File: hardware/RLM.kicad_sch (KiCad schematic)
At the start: 24 parts, among them J1 Conn_01x03, J2 Conn_01x03, SW1 SW_Push, SW2 SW_Push, U3 AP1117-33, U7 MCP2562-E-SN

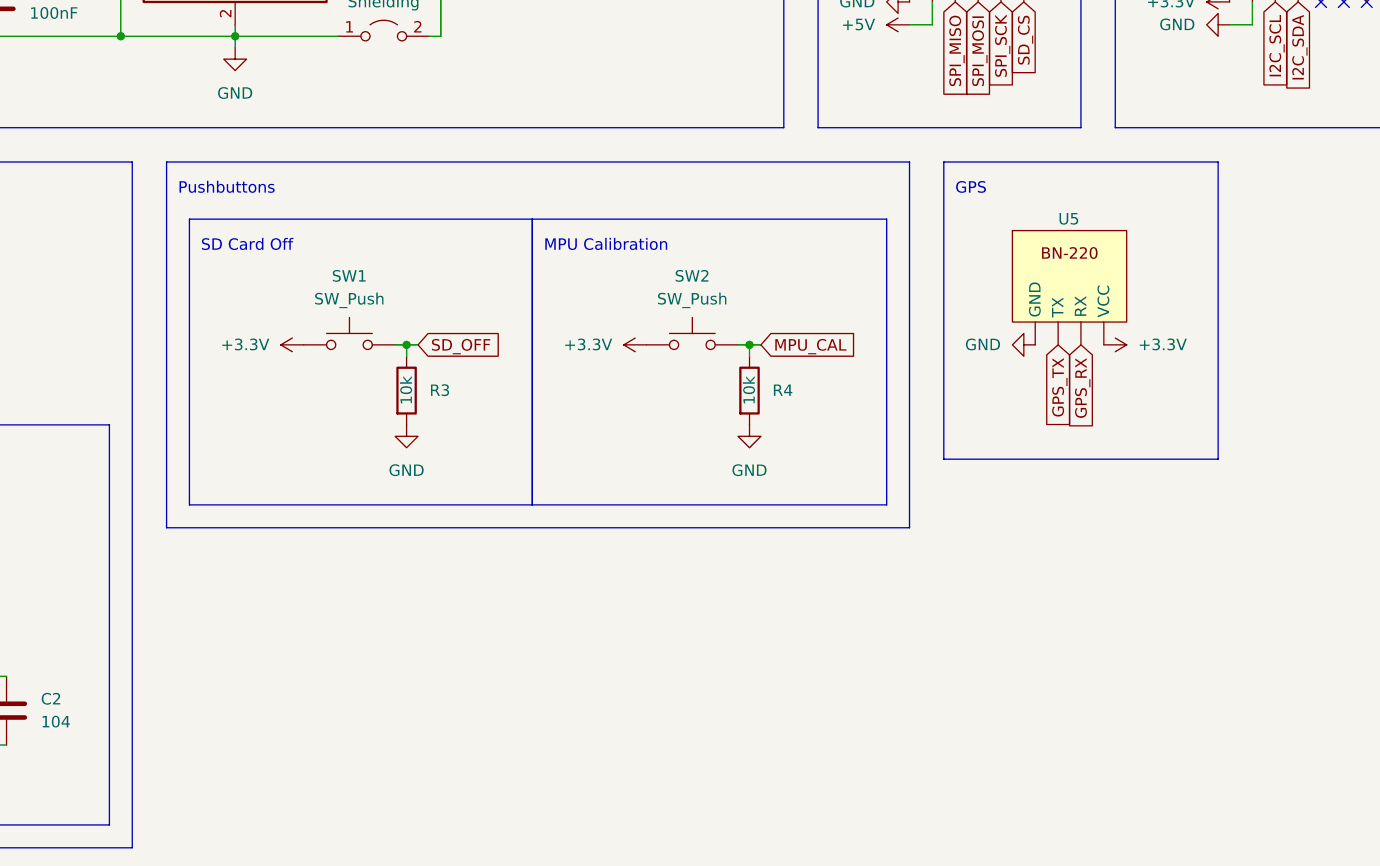
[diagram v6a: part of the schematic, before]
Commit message: feat: add mounting holes
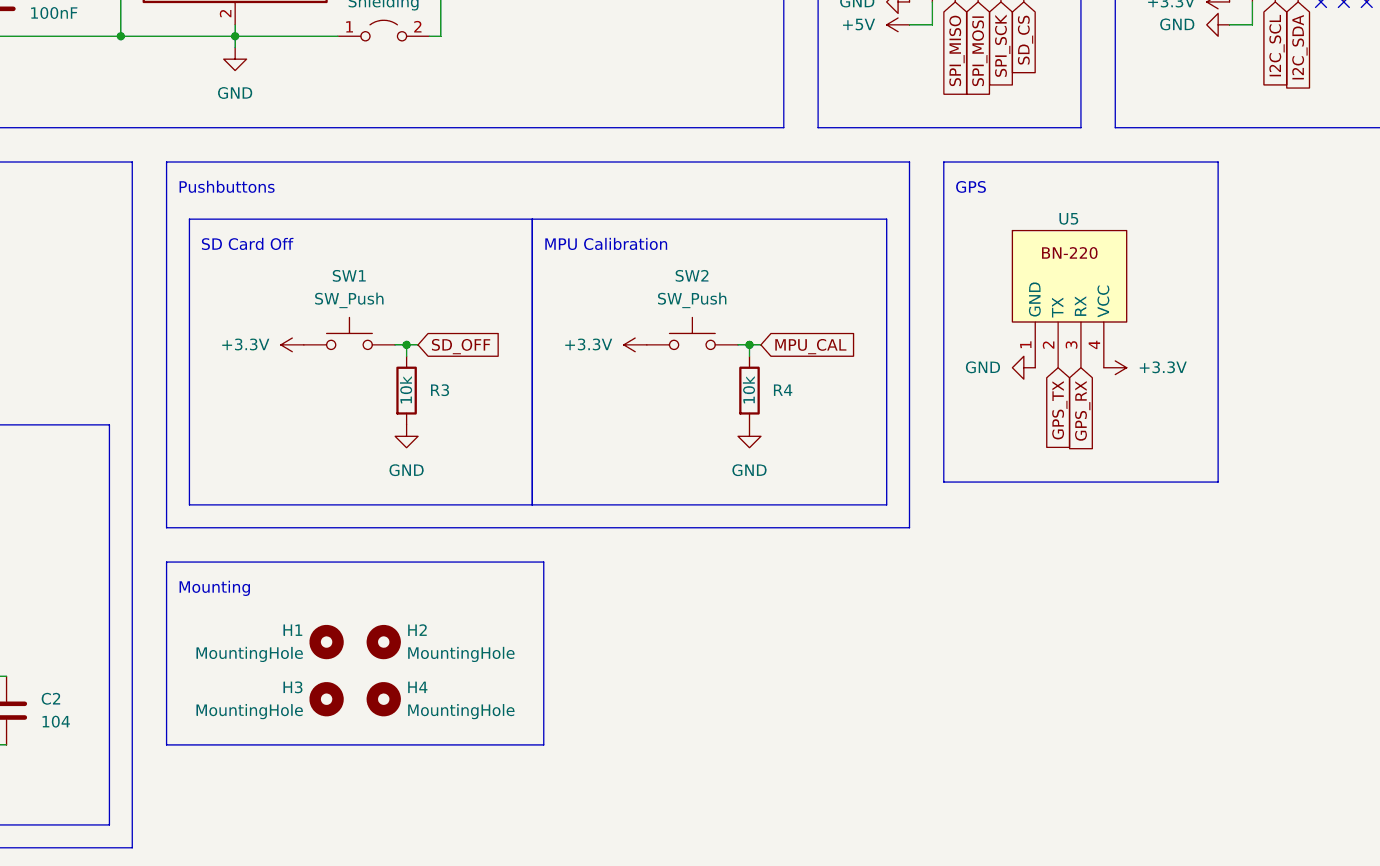
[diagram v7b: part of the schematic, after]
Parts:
- added H1, H2, H3, H4: MountingHole, MountingHole:MountingHole_4.3mm_M4, symbol Mechanical:MountingHole
- R3, R4: footprint (none) -> Resistor_SMD:R_0603_1608Metric
- U5: footprint (none) -> Connector_PinHeader_2.54mm:PinHeader_1x04_P2.54mm_Vertical
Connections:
- net +3.3V: now also U5.4 (VCC); no longer U5. (VCC)
- net GND: now also U5.1 (GND); no longer U5. (VCC)
- net GPS_RX: now also U5.3 (RX); no longer U5. (VCC)
- net GPS_TX: now also U5.2 (TX); no longer U5. (VCC)
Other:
- note added: "Mounting"
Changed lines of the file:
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@@
     (fill (type none))
   )
-  (rectangle (start 204.47 95.25) (end 234.95 128.27)
+  (rectangle (start 204.47 95.25) (end 234.95 130.81)
     (stroke (width 0) (type default))
     (fill (type none))
@@
     (fill (type none))
   )
+  (rectangle (start 118.11 139.7) (end 160.02 160.02)
+    (stroke (width 0) (type default))
+    (fill (type none))
+  )
   (rectangle (start 17.78 17.78) (end 76.2 91.44)
     (stroke (width 0) (type default))
@@
     (effects (font (size 1.27 1.27)) (justify left bottom))
   )
+  (text "Mounting" (at 119.38 143.51 0)
+    (effects (font (size 1.27 1.27)) (justify left bottom))
+  )
   (text "Accelerometer/Gyroscope" (at 224.79 55.88 0)
     (effects (font (size 1.27 1.27)) (justify left bottom))
@@
     )
   )
-  (global_label "GPS_RX" (shape input) (at 219.71 115.57 270) (fields_autoplaced)
-    (effects (font (size 1.27 1.27)) (justify right))
-    (property "Intersheetrefs" "${INTERSHEET_REFS}" (at 219.71 125.7518 90)
+  (global_label "GPS_RX" (shape input) (at 219.71 118.11 270) (fields_autoplaced)
+    (effects (font (size 1.27 1.27)) (justify right))
+    (property "Intersheetrefs" "${INTERSHEET_REFS}" (at 219.71 128.2918 90)
       (effects (font (size 1.27 1.27)) (justify right) hide)
     )
@@
     )
   )
-  (global_label "GPS_TX" (shape input) (at 217.17 115.57 270) (fields_autoplaced)
-    (effects (font (size 1.27 1.27)) (justify right))
-    (property "Intersheetrefs" "${INTERSHEET_REFS}" (at 217.17 125.4494 90)
+  (global_label "GPS_TX" (shape input) (at 217.17 118.11 270) (fields_autoplaced)
+    (effects (font (size 1.27 1.27)) (justify right))
+    (property "Intersheetrefs" "${INTERSHEET_REFS}" (at 217.17 127.9894 90)
       (effects (font (size 1.27 1.27)) (justify right) hide)
     )
@@
     )
   )
-  (symbol (lib_id "power:+3.3V") (at 222.25 115.57 270) (unit 1)
-    (in_bom yes) (on_board yes) (dnp no) (fields_autoplaced)
-    (property "Reference" "#PWR08" (at 218.44 115.57 0)
-      (effects (font (size 1.27 1.27)) hide)
-    )
-    (property "Value" "+3.3V" (at 226.06 115.57 90)
-      (effects (font (size 1.27 1.27)) (justify left))
-    )
-    (property "Footprint" "" (at 222.25 115.57 0)
-      (effects (font (size 1.27 1.27)) hide)
-    )
-    (property "Datasheet" "" (at 222.25 115.57 0)
+  (symbol (lib_id "power:+3.3V") (at 222.25 118.11 270) (unit 1)
+    (in_bom yes) (on_board yes) (dnp no) (fields_autoplaced)
+    (property "Reference" "#PWR08" (at 218.44 118.11 0)
+      (effects (font (size 1.27 1.27)) hide)
+    )
+    (property "Value" "+3.3V" (at 226.06 118.11 90)
+      (effects (font (size 1.27 1.27)) (justify left))
+    )
+    (property "Footprint" "" (at 222.25 118.11 0)
+      (effects (font (size 1.27 1.27)) hide)
+    )
+    (property "Datasheet" "" (at 222.25 118.11 0)
       (effects (font (size 1.27 1.27)) hide)
     )
@@
         (path "/3fe8a1ac-6190-4220-82eb-f4588302947e"
           (reference "#PWR04") (unit 1)
+        )
+      )
+    )
+  )
+  (symbol (lib_id "Mechanical:MountingHole") (at 142.24 154.94 0) (unit 1)
+    (in_bom yes) (on_board yes) (dnp no) (fields_autoplaced)
+    (property "Reference" "H4" (at 144.78 153.67 0)
+      (effects (font (size 1.27 1.27)) (justify left))
+    )
+    (property "Value" "MountingHole" (at 144.78 156.21 0)
+      (effects (font (size 1.27 1.27)) (justify left))
+    )
+    (property "Footprint" "MountingHole:MountingHole_4.3mm_M4" (at 142.24 154.94 0)
+      (effects (font (size 1.27 1.27)) hide)
+    )
+    (property "Datasheet" "~" (at 142.24 154.94 0)
+      (effects (font (size 1.27 1.27)) hide)
+    )
+    (instances
+      (project "RLM"
+        (path "/3fe8a1ac-6190-4220-82eb-f4588302947e"
+          (reference "H4") (unit 1)
         )
       )
@@
     )
   )
-  (symbol (lib_id "power:GND") (at 214.63 115.57 270) (unit 1)
-    (in_bom yes) (on_board yes) (dnp no) (fields_autoplaced)
-    (property "Reference" "#PWR09" (at 208.28 115.57 0)
-      (effects (font (size 1.27 1.27)) hide)
-    )
-    (property "Value" "GND" (at 210.82 115.57 90)
+  (symbol (lib_id "power:GND") (at 214.63 118.11 270) (unit 1)
+    (in_bom yes) (on_board yes) (dnp no) (fields_autoplaced)
+    (property "Reference" "#PWR09" (at 208.28 118.11 0)
+      (effects (font (size 1.27 1.27)) hide)
+    )
+    (property "Value" "GND" (at 210.82 118.11 90)
       (effects (font (size 1.27 1.27)) (justify right))
     )
-    (property "Footprint" "" (at 214.63 115.57 0)
-      (effects (font (size 1.27 1.27)) hide)
-    )
-    (property "Datasheet" "" (at 214.63 115.57 0)
+    (property "Footprint" "" (at 214.63 118.11 0)
+      (effects (font (size 1.27 1.27)) hide)
+    )
+    (property "Datasheet" "" (at 214.63 118.11 0)
       (effects (font (size 1.27 1.27)) hide)
     )
@@
     )
   )
+  (symbol (lib_id "Mechanical:MountingHole") (at 135.89 154.94 0) (unit 1)
+    (in_bom yes) (on_board yes) (dnp no)
+    (property "Reference" "H3" (at 133.35 153.67 0)
+      (effects (font (size 1.27 1.27)) (justify right))
+    )
+    (property "Value" "MountingHole" (at 133.35 156.21 0)
+      (effects (font (size 1.27 1.27)) (justify right))
+    )
+    (property "Footprint" "MountingHole:MountingHole_4.3mm_M4" (at 135.89 154.94 0)
+      (effects (font (size 1.27 1.27)) hide)
+    )
+    (property "Datasheet" "~" (at 135.89 154.94 0)
+      (effects (font (size 1.27 1.27)) hide)
+    )
+    (instances
+      (project "RLM"
+        (path "/3fe8a1ac-6190-4220-82eb-f4588302947e"
+          (reference "H3") (unit 1)
+        )
+      )
+    )
+  )
   (symbol (lib_id "Device:LED") (at 25.4 146.05 90) (unit 1)
     (in_bom yes) (on_board yes) (dnp no)
@@
     )
   )
+  (symbol (lib_id "Mechanical:MountingHole") (at 135.89 148.59 0) (unit 1)
+    (in_bom yes) (on_board yes) (dnp no)
+    (property "Reference" "H1" (at 133.35 147.32 0)
+      (effects (font (size 1.27 1.27)) (justify right))
+    )
+    (property "Value" "MountingHole" (at 133.35 149.86 0)
+      (effects (font (size 1.27 1.27)) (justify right))
+    )
+    (property "Footprint" "MountingHole:MountingHole_4.3mm_M4" (at 135.89 148.59 0)
+      (effects (font (size 1.27 1.27)) hide)
+    )
+    (property "Datasheet" "~" (at 135.89 148.59 0)
+      (effects (font (size 1.27 1.27)) hide)
+    )
+    (instances
+      (project "RLM"
+        (path "/3fe8a1ac-6190-4220-82eb-f4588302947e"
+          (reference "H1") (unit 1)
+        )
+      )
+    )
+  )
   (symbol (lib_id "power:+5V") (at 200.66 80.01 90) (unit 1)
     (in_bom yes) (on_board yes) (dnp no) (fields_autoplaced)
@@
       (effects (font (size 1.27 1.27)))
     )
-    (property "Footprint" "" (at 181.102 120.65 90)
+    (property "Footprint" "Resistor_SMD:R_0603_1608Metric" (at 181.102 120.65 90)
       (effects (font (size 1.27 1.27)) hide)
     )
@@
       (effects (font (size 1.27 1.27)))
     )
-    (property "Footprint" "" (at 218.44 102.87 0)
+    (property "Footprint" "Connector_PinHeader_2.54mm:PinHeader_1x04_P2.54mm_Vertical" (at 218.44 102.87 0)
       (effects (font (size 1.27 1.27)) hide)
     )
@@
       (effects (font (size 1.27 1.27)) hide)
     )
-    (pin "")
-    (pin "")
-    (pin "")
-    (pin "")
+    (pin "1")
+    (pin "2")
+    (pin "3")
+    (pin "4")
     (instances
       (project "RLM"
@@
         (path "/3fe8a1ac-6190-4220-82eb-f4588302947e"
           (reference "C5") (unit 1)
+        )
+      )
+    )
+  )
+  (symbol (lib_id "Mechanical:MountingHole") (at 142.24 148.59 0) (unit 1)
+    (in_bom yes) (on_board yes) (dnp no) (fields_autoplaced)
+    (property "Reference" "H2" (at 144.78 147.32 0)
+      (effects (font (size 1.27 1.27)) (justify left))
+    )
+    (property "Value" "MountingHole" (at 144.78 149.86 0)
+      (effects (font (size 1.27 1.27)) (justify left))
+    )
+    (property "Footprint" "MountingHole:MountingHole_4.3mm_M4" (at 142.24 148.59 0)
+      (effects (font (size 1.27 1.27)) hide)
+    )
+    (property "Datasheet" "~" (at 142.24 148.59 0)
+      (effects (font (size 1.27 1.27)) hide)
+    )
+    (instances
+      (project "RLM"
+        (path "/3fe8a1ac-6190-4220-82eb-f4588302947e"
+          (reference "H2") (unit 1)
         )
       )
@@
       (effects (font (size 1.27 1.27)))
     )
-    (property "Footprint" "" (at 143.002 120.65 90)
-      (effects (font (size 1.27 1.27)) hide)
-    )
+    (property "Footprint" "Resistor_SMD:R_0603_1608Metric" (at 143.002 120.65 90)
+      (effects (font (size 1.27 1.27)) hide)
+    )

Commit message: feat: layout v2
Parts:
- H1, H2, H3, H4: footprint MountingHole:MountingHole_4.3mm_M4 -> MountingHole:MountingHole_4.3mm_M4_ISO14580_Pad
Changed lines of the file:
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@@
       (effects (font (size 1.27 1.27)) (justify left))
     )
-    (property "Footprint" "MountingHole:MountingHole_4.3mm_M4" (at 142.24 154.94 0)
+    (property "Footprint" "MountingHole:MountingHole_4.3mm_M4_ISO14580_Pad" (at 142.24 154.94 0)
       (effects (font (size 1.27 1.27)) hide)
     )
@@
       (effects (font (size 1.27 1.27)) (justify right))
     )
-    (property "Footprint" "MountingHole:MountingHole_4.3mm_M4" (at 135.89 154.94 0)
+    (property "Footprint" "MountingHole:MountingHole_4.3mm_M4_ISO14580_Pad" (at 135.89 154.94 0)
       (effects (font (size 1.27 1.27)) hide)
     )
@@
       (effects (font (size 1.27 1.27)) (justify right))
     )
-    (property "Footprint" "MountingHole:MountingHole_4.3mm_M4" (at 135.89 148.59 0)
+    (property "Footprint" "MountingHole:MountingHole_4.3mm_M4_ISO14580_Pad" (at 135.89 148.59 0)
       (effects (font (size 1.27 1.27)) hide)
     )
@@
       (effects (font (size 1.27 1.27)) (justify left))
     )
-    (property "Footprint" "MountingHole:MountingHole_4.3mm_M4" (at 142.24 148.59 0)
-      (effects (font (size 1.27 1.27)) hide)
-    )
+    (property "Footprint" "MountingHole:MountingHole_4.3mm_M4_ISO14580_Pad" (at 142.24 148.59 0)
+      (effects (font (size 1.27 1.27)) hide)
+    )
